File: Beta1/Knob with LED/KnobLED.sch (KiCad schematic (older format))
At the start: 0 parts

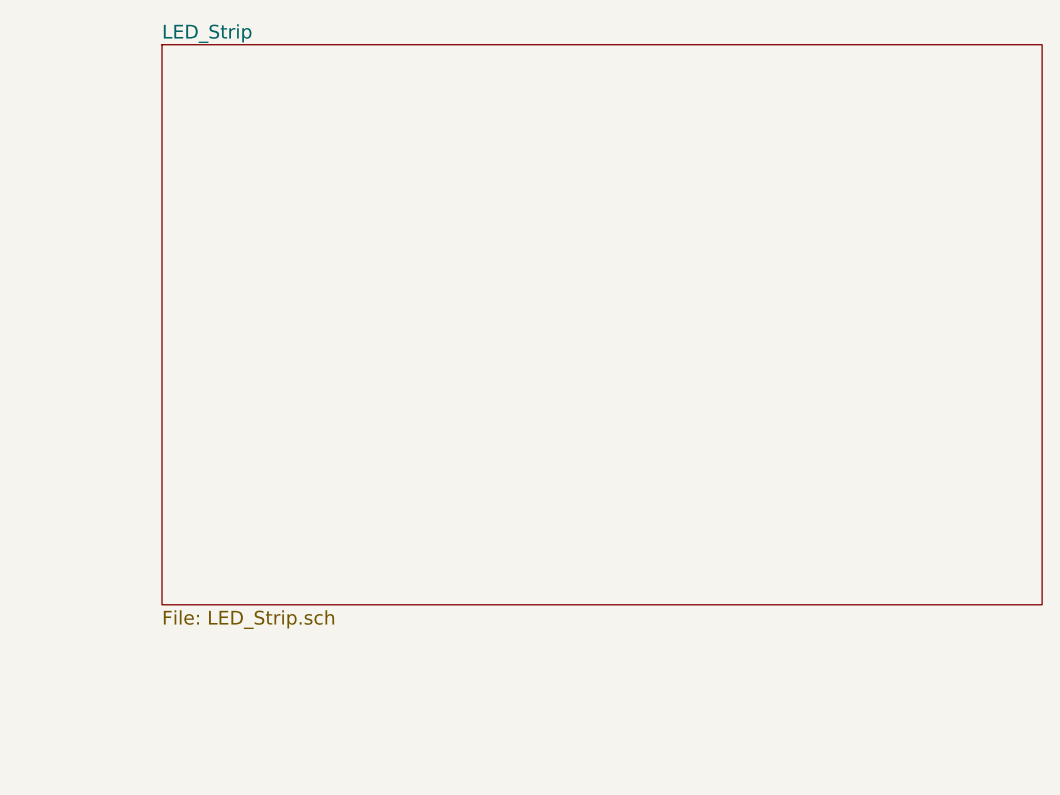
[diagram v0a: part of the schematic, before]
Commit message: Placed all LED strip components. Only routing remains
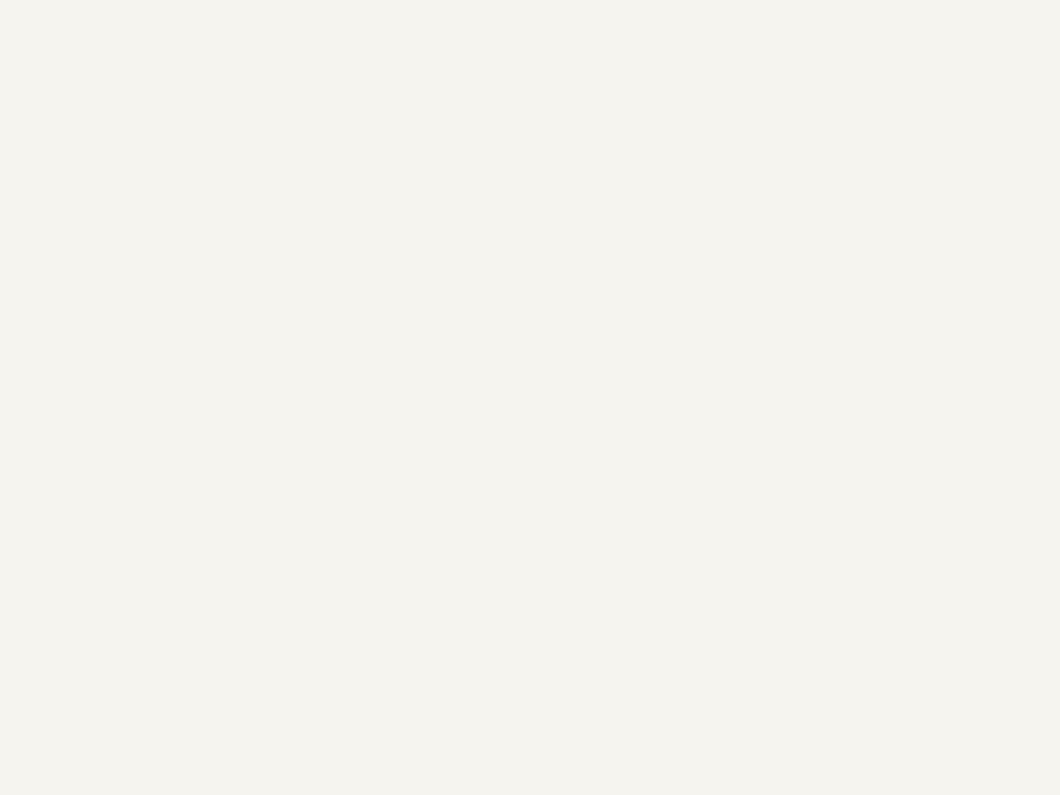
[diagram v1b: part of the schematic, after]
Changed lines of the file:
@@
 $Descr B 17000 11000
 encoding utf-8
-Sheet 1 3
+Sheet 1 2
 Title ""
 Date ""
@@
 $EndDescr
 $Sheet
-S 6300 1600 3850 2450
-U 582E4C4F
-F0 "LED_Strip" 60
-F1 "LED_Strip.sch" 60
-$EndSheet
-$Sheet
 S 4350 6050 3800 2250
